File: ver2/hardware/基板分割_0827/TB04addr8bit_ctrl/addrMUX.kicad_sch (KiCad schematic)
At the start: 14 parts, among them U1401 74HC138, U1402 74HC244, U1403 74HC244, U1404 74HC244, U1405 74HC244, U1406 74LS157, U1407 74LS139

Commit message: ver2: 3分割の74LS表記をHCへ一括変更(31パッケージ・Valueのみ)
- 書き換えたのはValueプロパティのみ(56件=31パッケージ)
- lib_id(74xx:74LS***)とDatasheetは変更せず。HC品のシンボルがKiCADに
  無いため、lib_idを変えるとシンボル未検出になる
- 74LS->74HCの単純置換で9品種すべて実在の型番(00/08/10/32/139/157/
  253/273/377)。ピン配置は同一でネットリストへの影響なし

検証: 残存する74LSのValue 0件、git diffの変更行はValueの56行のみ
申し送り: PCB側のValueは未同期。「回路図からPCBを更新」で解消する

Co-Authored-By: Claude Opus 5 <noreply@anthropic.com>
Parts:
- U1406: value 74LS157 -> 74HC157
- U1407: value 74LS139 -> 74HC139
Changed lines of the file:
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@@
 			)
 		)
-		(property "Value" "74LS139"
+		(property "Value" "74HC139"
 			(at 273.05 133.35 0)
 			(show_name no)
@@
 			)
 		)
-		(property "Value" "74LS139"
+		(property "Value" "74HC139"
 			(at 242.57 256.5399 0)
 			(show_name no)
@@
 			)
 		)
-		(property "Value" "74LS139"
+		(property "Value" "74HC139"
 			(at 271.78 106.68 0)
 			(show_name no)
@@
 			)
 		)
-		(property "Value" "74LS157"
+		(property "Value" "74HC157"
 			(at 181.2133 106.68 0)
 			(show_name no)

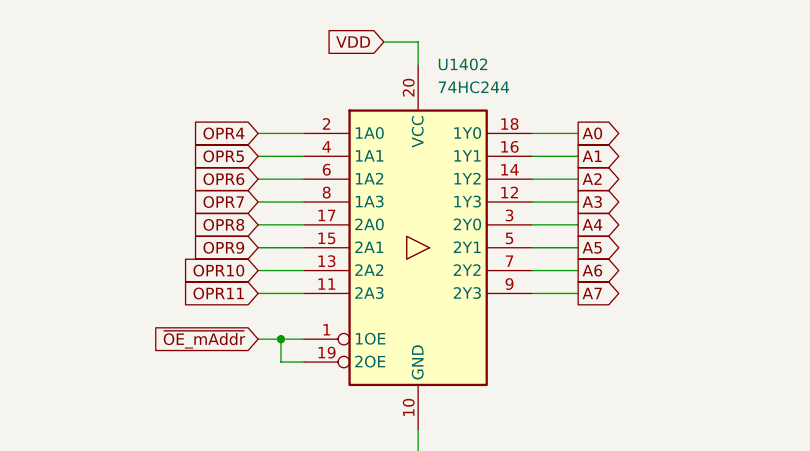
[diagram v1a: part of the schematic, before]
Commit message: ver2: 制御板のピン割当(案C)を適用(6IC・44ピン入替で交差-17.7%)
74HC244×3(U1102/U1103/U1402)・74HC157×3(U101/U401/U404)でバスのビット順を入替。
検証は全項目合格＝変化は44パッドのみ・244の(A,Y)対と157の(A,B,Y)三つ組は集合一致・
制御ピン不変・ネットの構成部品変化0・DRC/schematic parityはHEADと項目単位で完全一致。
HPWL +0.16%(15,542→15,567mm)。配置と外形は不動。

Co-Authored-By: Claude Opus 5 <noreply@anthropic.com>
Claude-Session: https://claude.ai/code/session_01FHQyZznjPPN9g6quxMNLGo
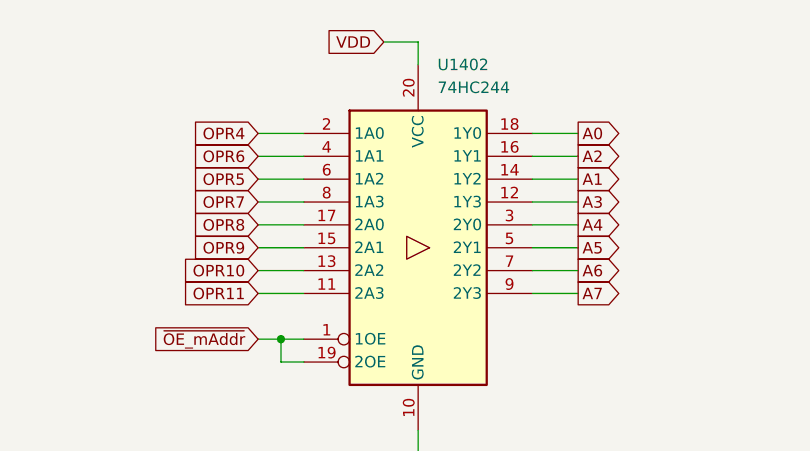
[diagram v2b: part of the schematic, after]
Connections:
- net A1: now also U1402.14 (1Y2); no longer U1402.16 (1Y1)
- net A2: now also U1402.16 (1Y1); no longer U1402.14 (1Y2)
- net OPR5: now also U1402.6 (1A2); no longer U1402.4 (1A1)
- net OPR6: now also U1402.4 (1A1); no longer U1402.6 (1A2)
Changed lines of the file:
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@@
 	(wire
 		(pts
+			(xy 217.17 38.1) (xy 222.25 38.1)
+		)
+		(stroke
+			(width 0)
+			(type default)
+		)
+	)
+	(wire
+		(pts
 			(xy 356.87 203.2) (xy 361.95 203.2)
 		)
@@
 	(wire
 		(pts
+			(xy 247.65 38.1) (xy 252.73 38.1)
+		)
+		(stroke
+			(width 0)
+			(type default)
+		)
+	)
+	(wire
+		(pts
 			(xy 162.56 129.54) (xy 166.37 129.54)
 		)
@@
 	(wire
 		(pts
-			(xy 222.25 60.96) (xy 219.71 60.96)
+			(xy 247.65 40.64) (xy 252.73 40.64)
 		)
 		(stroke
@@
 	(wire
 		(pts
-			(xy 170.18 44.45) (xy 175.26 44.45)
+			(xy 222.25 60.96) (xy 219.71 60.96)
 		)
 		(stroke
@@
 	(wire
 		(pts
-			(xy 322.58 48.26) (xy 318.77 48.26)
+			(xy 170.18 44.45) (xy 175.26 44.45)
 		)
 		(stroke
@@
 	(wire
 		(pts
-			(xy 86.36 129.54) (xy 91.44 129.54)
+			(xy 322.58 48.26) (xy 318.77 48.26)
 		)
 		(stroke
@@
 	(wire
 		(pts
-			(xy 288.29 114.3) (xy 284.48 114.3)
+			(xy 86.36 129.54) (xy 91.44 129.54)
 		)
 		(stroke
@@
 	(wire
 		(pts
-			(xy 53.34 71.12) (xy 66.04 71.12)
+			(xy 288.29 114.3) (xy 284.48 114.3)
 		)
 		(stroke
@@
 	(wire
 		(pts
-			(xy 217.17 38.1) (xy 222.25 38.1)
+			(xy 53.34 71.12) (xy 66.04 71.12)
 		)
 		(stroke
@@
 	(wire
 		(pts
-			(xy 247.65 38.1) (xy 252.73 38.1)
-		)
-		(stroke
-			(width 0)
-			(type default)
-		)
-	)
-	(wire
-		(pts
 			(xy 387.35 224.79) (xy 373.38 224.79)
 		)
@@
 	(wire
 		(pts
+			(xy 217.17 40.64) (xy 222.25 40.64)
+		)
+		(stroke
+			(width 0)
+			(type default)
+		)
+	)
+	(wire
+		(pts
 			(xy 217.17 53.34) (xy 222.25 53.34)
 		)
@@
 	(wire
 		(pts
-			(xy 217.17 40.64) (xy 222.25 40.64)
-		)
-		(stroke
-			(width 0)
-			(type default)
-		)
-	)
-	(wire
-		(pts
 			(xy 144.78 54.61) (xy 139.7 54.61)
 		)
@@
 	(wire
 		(pts
-			(xy 247.65 40.64) (xy 252.73 40.64)
-		)
-		(stroke
-			(width 0)
-			(type default)
-		)
-	)
-	(wire
-		(pts
 			(xy 66.04 71.12) (xy 66.04 66.04)
 		)
@@
 	(global_label "OPR6"
 		(shape input)
-		(at 217.17 40.64 180)
+		(at 217.17 38.1 180)
 		(fields_autoplaced yes)
 		(effects
@@
 		)
 		(property "Intersheetrefs" "${INTERSHEET_REFS}"
-			(at 209.1048 40.64 0)
+			(at 209.1048 38.1 0)
 			(show_name no)
 			(do_not_autoplace no)
@@
 	(global_label "A1"
 		(shape output)
-		(at 252.73 38.1 0)
+		(at 252.73 40.64 0)
 		(fields_autoplaced yes)
 		(effects
@@
 		)
 		(property "Intersheetrefs" "${INTERSHEET_REFS}"
-			(at 258.0133 38.1 0)
+			(at 258.0133 40.64 0)
 			(show_name no)
 			(do_not_autoplace no)
@@
 	(global_label "A2"
 		(shape output)
-		(at 252.73 40.64 0)
+		(at 252.73 38.1 0)
 		(fields_autoplaced yes)
 		(effects
@@
 		)
 		(property "Intersheetrefs" "${INTERSHEET_REFS}"
-			(at 258.0133 40.64 0)
+			(at 258.0133 38.1 0)
 			(show_name no)
 			(do_not_autoplace no)
@@
 	(global_label "OPR5"
 		(shape input)
-		(at 217.17 38.1 180)
+		(at 217.17 40.64 180)
 		(fields_autoplaced yes)
 		(effects
@@
 		)
 		(property "Intersheetrefs" "${INTERSHEET_REFS}"
-			(at 209.1048 38.1 0)
+			(at 209.1048 40.64 0)
 			(show_name no)
 			(do_not_autoplace no)

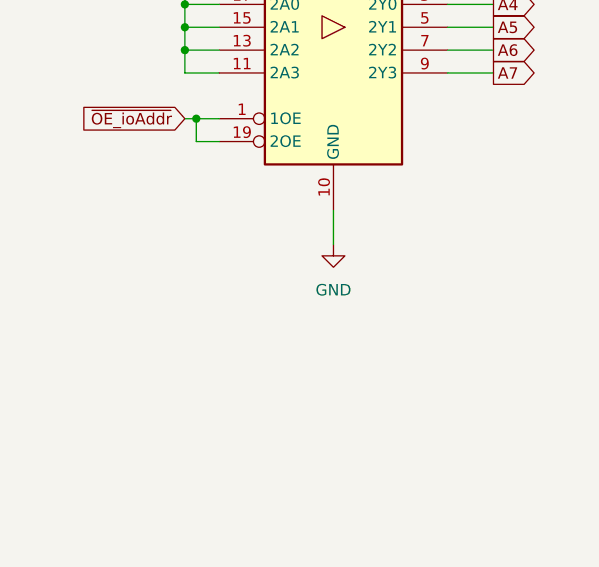
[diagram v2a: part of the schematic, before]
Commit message: ver2: 制御板の回路図にU1405の注記を追加しSP系ラベルを整理
addrMUXにU1405(I/Oアドレス退避用244)の役割を注記。gatesのSP系
グローバルラベル7個をワイヤ結線に置換。署名比較で839ピン・変化0
・構成員集合160組とも一致＝電気的変更なし。

Co-Authored-By: Claude Opus 5 <noreply@anthropic.com>
Claude-Session: https://claude.ai/code/session_01WTj4Rxd6mdq2KnsBbdjqBt
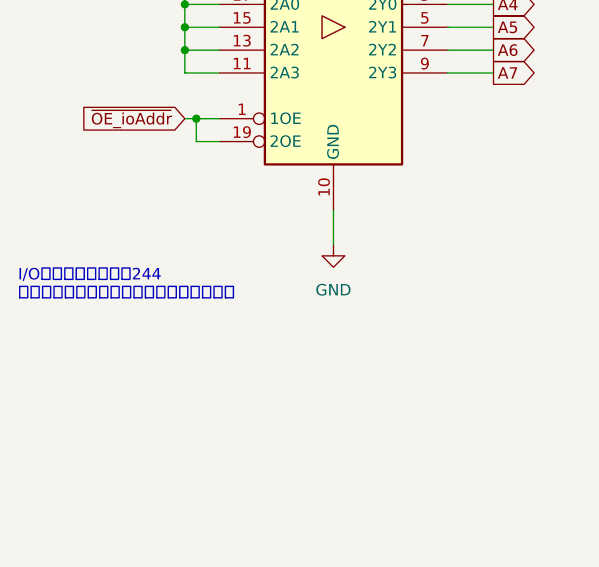
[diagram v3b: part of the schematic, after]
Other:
- note added: "I/Oチャネル指定用の244 他のアドレスを選択しないようにしている"
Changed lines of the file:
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@@
+		)
+	)
+	(text "I/Oチャネル指定用の244\n他のアドレスを選択しないようにしている"
+		(exclude_from_sim no)
+		(at 38.608 158.242 0)
+		(effects
+			(font
+				(size 1.27 1.27)
+			)
+			(justify left)
 		)
 	)
